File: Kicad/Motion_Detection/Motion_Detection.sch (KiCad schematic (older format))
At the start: 19 parts, among them J1 SEN0192_MW, J2 SE-10, J3 12V input, J4 5V Ext, J5 3V3 EN, J6 ZRE200GE, J7 EKMB, J8 3V3 Output, P1 XBee, U1 LM324, U2 LM7805_TO220

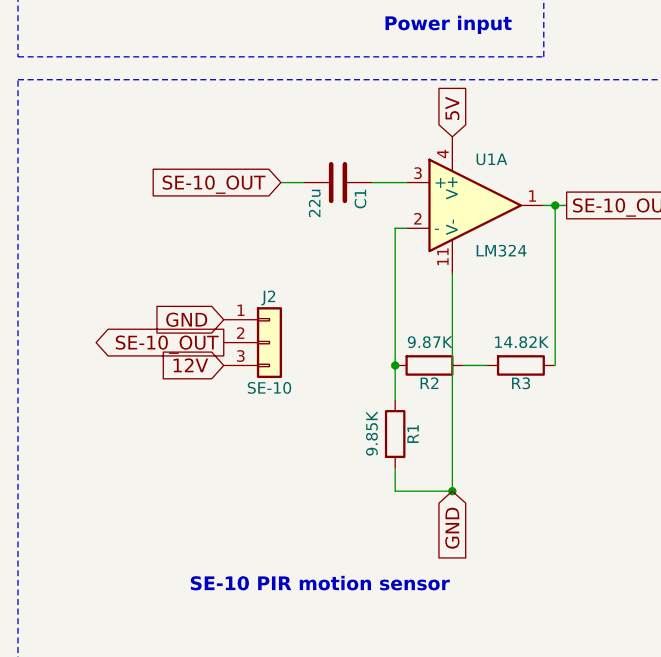
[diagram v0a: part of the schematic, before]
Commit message: Updated Kicad Motion detection circuit and board. Updated Feather code to comunicate using XBee.
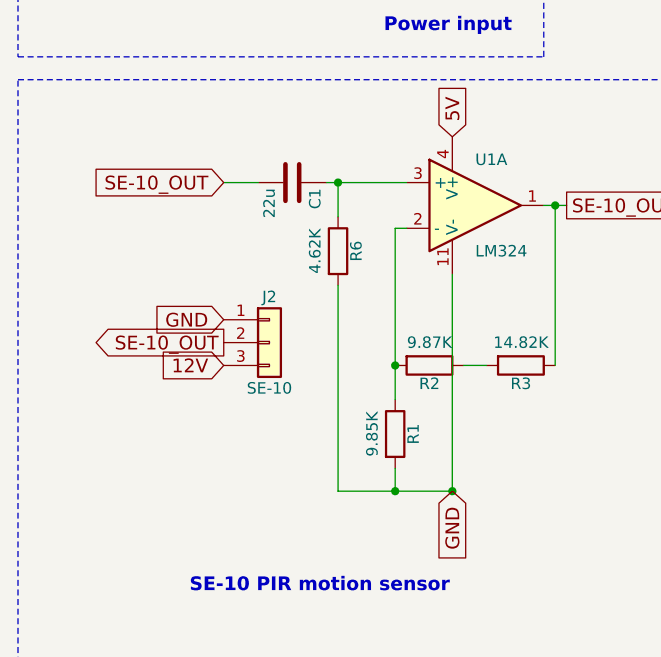
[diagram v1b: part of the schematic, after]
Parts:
- added R6: 4.62K, Resistors_THT:R_Axial_DIN0207_L6.3mm_D2.5mm_P7.62mm_Horizontal, symbol R
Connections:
- net GND: now also R6.2
- net at C1.1, U1.3 (+): now also R6.1
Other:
- moved on the sheet: C1
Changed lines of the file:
@@
 Text GLabel 2400 2250 1    60   Input ~ 0
 5V
-Text GLabel 1650 2450 0    60   Input ~ 0
+Text GLabel 1400 2450 0    60   Input ~ 0
 SE-10_OUT
 $Comp
@@
 L C C1
 U 1 1 5A0C1F63
-P 1900 2450
-F 0 "C1" H 1925 2550 50  0000 L CNN
-F 1 "22u" H 1925 2350 50  0000 L CNN
-F 2 "Capacitors_THT:CP_Radial_D5.0mm_P2.50mm" H 1938 2300 50  0001 C CNN
-F 3 "" H 1900 2450 50  0001 C CNN
-	1    1900 2450
+P 1700 2450
+F 0 "C1" H 1725 2550 50  0000 L CNN
+F 1 "22u" H 1725 2350 50  0000 L CNN
+F 2 "Capacitors_THT:CP_Radial_D5.0mm_P2.50mm" H 1738 2300 50  0001 C CNN
+F 3 "" H 1700 2450 50  0001 C CNN
+	1    1700 2450
 	0    1    1    0
 $EndComp
@@
 	2150 3700 2150 3800
 Wire Wire Line
-	2150 3800 2400 3800
+	1900 3800 2400 3800
 Wire Wire Line
 	1000 1050 1000 1000
@@
 	7300 550  4000 550
 Wire Wire Line
-	2200 2450 2050 2450
-Wire Wire Line
-	1750 2450 1650 2450
+	2200 2450 1850 2450
+Wire Wire Line
+	1550 2450 1400 2450
 Wire Notes Line
 	7550 550  7550 6500
@@
 Text Notes 5500 7100 2    60   ~ 12
 XBee
+$Comp
+L R R6
+U 1 1 5A0DEF5A
+P 1900 2750
+F 0 "R6" V 1980 2750 50  0000 C CNN
+F 1 "4.62K" V 1800 2750 50  0000 C CNN
+F 2 "Resistors_THT:R_Axial_DIN0207_L6.3mm_D2.5mm_P7.62mm_Horizontal" V 1830 2750 50  0001 C CNN
+F 3 "" H 1900 2750 50  0001 C CNN
+	1    1900 2750
+	1    0    0    -1
+$EndComp
+Wire Wire Line
+	1900 2450 1900 2600
+Connection ~ 1900 2450
+Wire Wire Line
+	1900 2900 1900 3800
+Connection ~ 2150 3800
 $EndSCHEMATC
